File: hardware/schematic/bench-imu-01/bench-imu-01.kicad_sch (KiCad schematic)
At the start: 48 parts, among them J1 USB4105-GH-A, J2 UART, J3 SWD, J4 PJ-102AH, M1 T-Motor_MN2206-13_conn, SW1 SW_PUSH, U1 STM32G031K8T6, U2 BMI270, U3 TLV75533PDBV, U4 USBLC6-2SC6, U5 DRV10983, U6 TPS26631PWPR

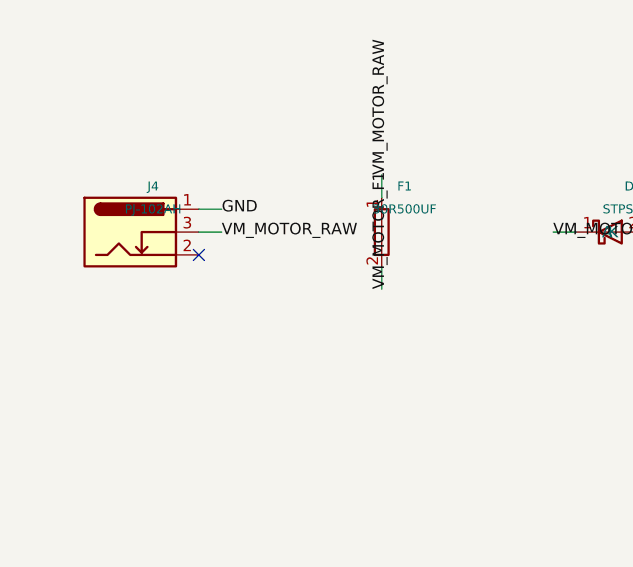
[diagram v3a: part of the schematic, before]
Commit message: PCB Engineer (at explicit Chief Engineer direction): attempt genuine design fix for ISS-032 (HIGH) -- add F2 GND-leg PTC fuse
Chief Engineer independently audited the CONDITIONAL PR (#17), confirmed
all claims, and gave explicit disposition on the 4 remaining open items:
continue iterating freely on ISS-031/036/037, but for ISS-032 (the
safety-critical J4 GND-hijack finding) -- "take a real crack at this as a
Circuit Engineer-level design question before treating this as an
escalation."

## The problem, precisely

J4 (barrel jack)'s tip/sleeve pin mapping is an ASSUMPTION (primary
datasheet's mechanical drawing not renderable by this session's
tooling). Before this fix: J4 pin1 (assumed sleeve/GND) tied DIRECTLY to
the shared ground net with zero protection, while J4 pin3 (assumed tip/+)
went through F1 (fuse) then D2 (series reverse-polarity diode). D2 only
ever protects against an EXTERNAL failure (a user plugging in a
reverse-polarity supply) -- it sits in the wrong leg to do anything about
an INTERNAL failure, where this design's own pin-mapping assumption is
simply wrong. If pin1/pin3 are actually swapped, the barrel jack's full
+9-13V supply would be applied directly to the shared ground reference
(used by the MCU, IMU, and J1's USB-C GND) with nothing in series to stop
it -- a real, previously undisclosed-as-such safety gap the design
documentation had actually overstated as covered by D2.

## The fix

Added F2: a second Littelfuse 30R500UF PTC resettable fuse, identical in
kind to F1 (same MPN, same DS-PROT-006/032/033 evidence), now in series
between J4's sleeve/GND pin and the shared ground net. This makes the
worst case safe REGARDLESS of which physical pin actually turns out to be
tip vs. sleeve, without ever needing to resolve that ASSUMPTION -- exactly
the property the Chief Engineer asked whether a second protective element
could achieve, and the reviewer's own ISS-032 finding text had already
suggested as an option ("add a second, independent protect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
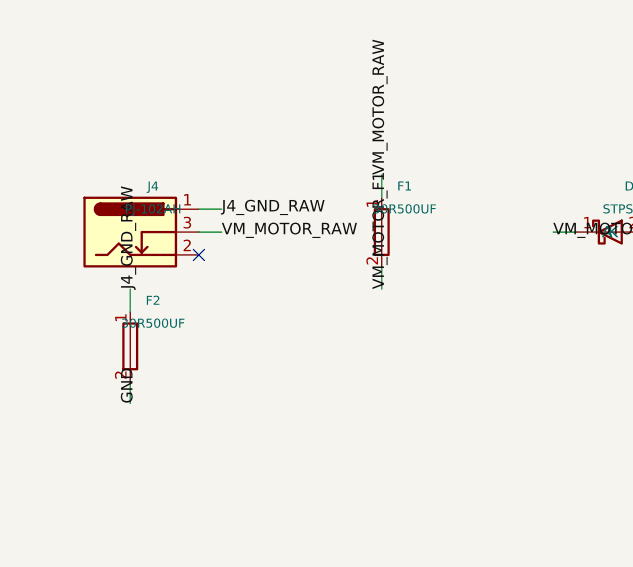
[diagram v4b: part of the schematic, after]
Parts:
- added F2: 30R500UF, bench-imu-01:Fuse_Littelfuse_30R500UF_Radial_D14.0mm_P10.2mm, symbol Device:Fuse
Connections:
- net GND: now also F2.2; no longer J4.1
- new net J4_GND_RAW: F2.1, J4.1

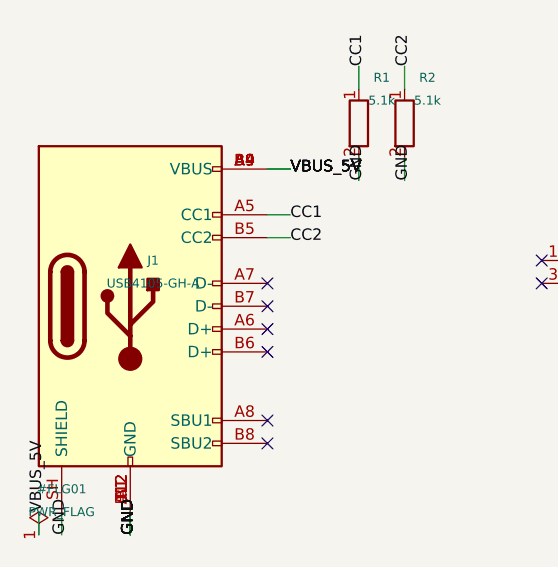
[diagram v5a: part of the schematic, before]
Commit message: Bench-IMU-01: fix J1's non-existent MPN USB4105-GH-A -> USB4105-GF-A (ISS-042, ECO-043)
J1's schematic symbol `Value` named `USB4105-GH-A`, a part number that does
not exist in GCT's catalog or at any distributor (independently re-verified
this session against DigiKey, Mouser and TME: only `USB4105-GF-A` and its
-060/-120 shell-stake variants are offered). It contradicted the CONFIRMED,
evidence-logged BOM MPN `USB4105-GF-A` (DS-CONN-007), and had been
propagated into the public GitHub Pages circuit viewer and its published
schematic PDF.

Root cause is the stale load-bearing figure propagation hazard documented in
docs/workflow.md 4.2: the value entered in 11eebfd (PR #9) as an openly
disclosed illustrative placeholder while J1's MPN was genuinely unselected;
PR #20 (2f64d8a) then resolved J1 to the real MPN across bom/,
datasheets/evidence-log.md, the DS-CONN-007 record and the PCB fab README,
but never back-propagated into the schematic symbol's own Value field, so
the placeholder survived silently and PR #25 republished it publicly.

Also fixes generate_schematic.py, which carried the same literal in its
b.place("J1", ...) call -- without it the defect would be reintroduced on
the next regeneration.

Not a component-selection decision: the correct value was already
human-visible and evidence-backed as CONFIRMED via DS-CONN-007. No net,
pin, footprint, placement, PCB, Gerber or BOM change -- the
USB4105-xx-A family land pattern was already correct for -GF-A.

Verified: pdftotext diff of old vs re-exported PDF = exactly one changed
line; 150-dpi pixel diff = one 72x7px region on a 2481x1754px page;
generate_schematic.py re-run and diffed with UUIDs normalized reproduces the
corrected .kicad_sch identically and differs from the previously-committed
one in exactly the J1 line; repo-wide re-scan of all 49 schematic Value
fields vs all 51 BOM rows = zero remaining non-existent MPNs; all three CI
gates green.

Co-authored-by: Copilot App <223556219+Copilot@users.norepl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
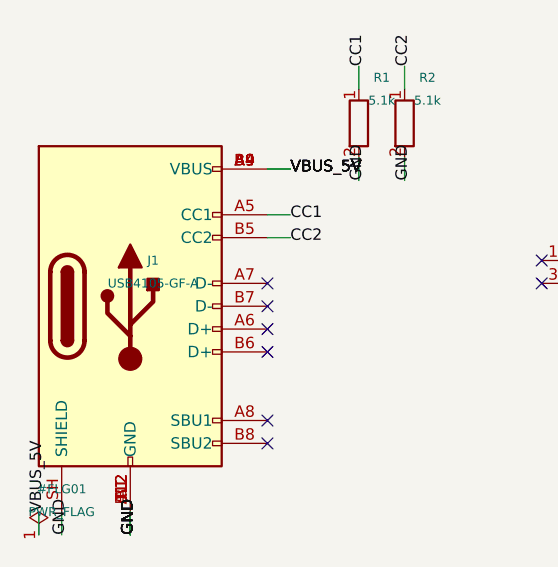
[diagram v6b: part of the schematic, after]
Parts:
- J1: value USB4105-GH-A -> USB4105-GF-A
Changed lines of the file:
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@@
       (effects (font (size 1.0 1.0)))
     )
-    (property "Value" "USB4105-GH-A" (id 1) (at 27.939999999999998 48.26 0)
+    (property "Value" "USB4105-GF-A" (id 1) (at 27.939999999999998 48.26 0)
       (effects (font (size 1.0 1.0)))
     )
